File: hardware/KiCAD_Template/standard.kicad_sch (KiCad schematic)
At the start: 40 parts, among them Q1 NMOS, Q2 NPN, SW1 SW_Push, SW2 SW_SPST, U1 ${SIM.PARAMS}

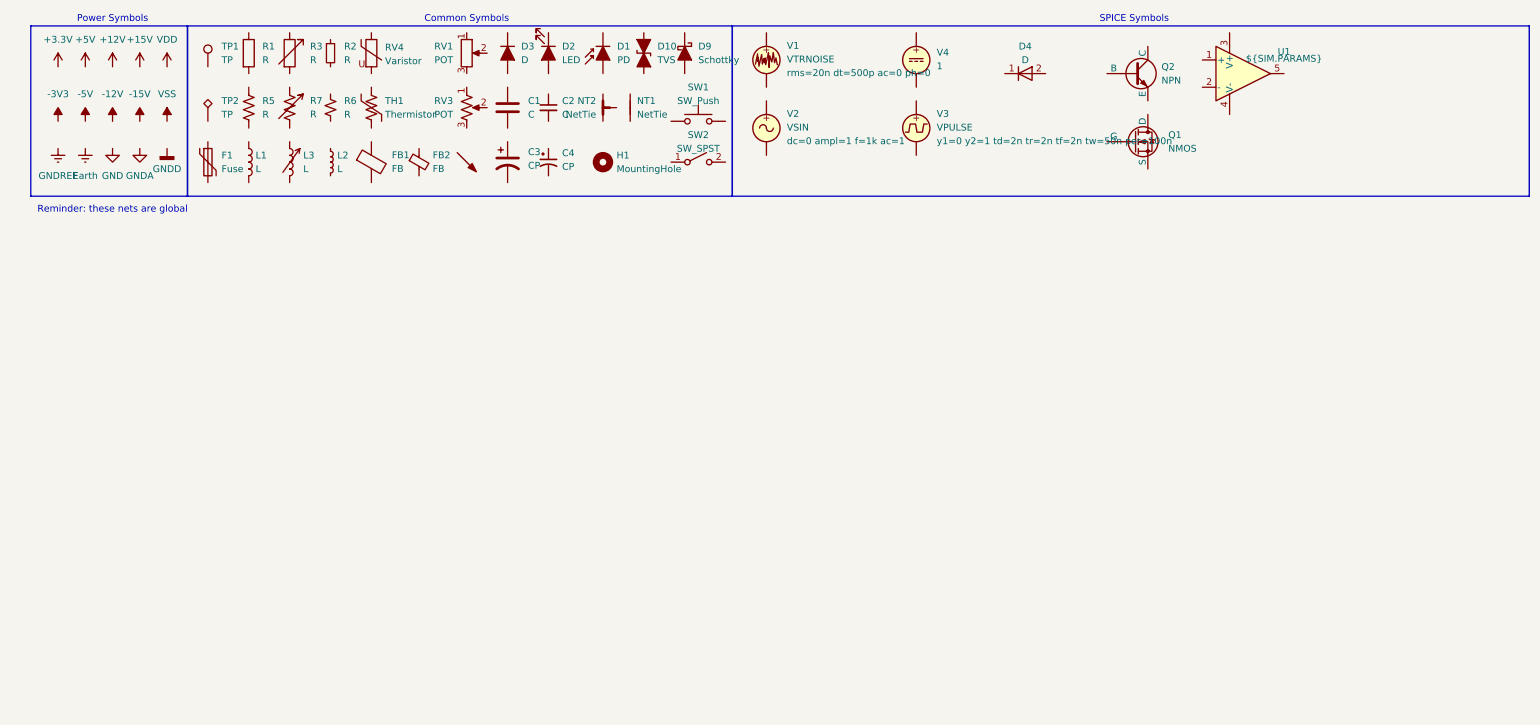
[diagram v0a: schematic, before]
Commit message: fix: kicad build automation output directory
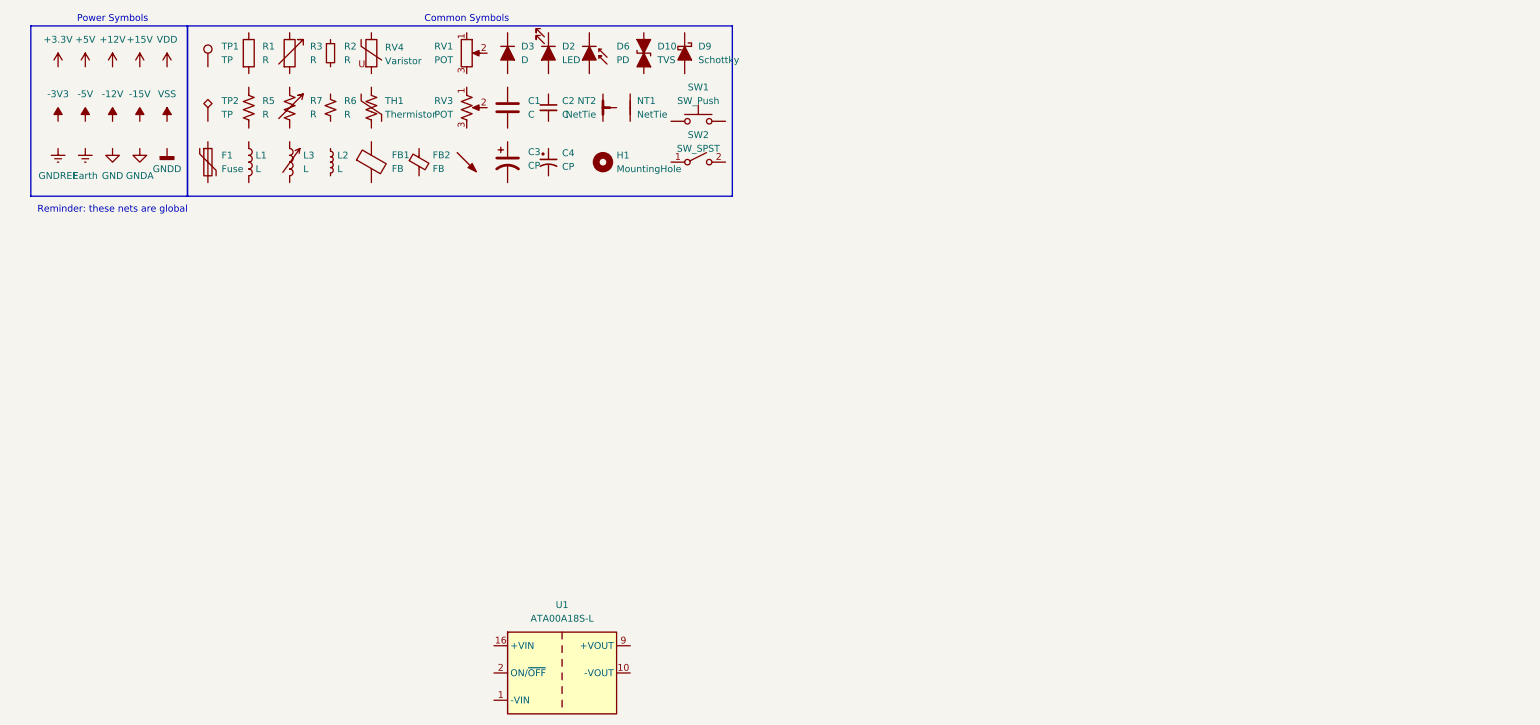
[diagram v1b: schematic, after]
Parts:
- removed D1: PD, symbol Device:D_Photo_Filled
- removed D4: D, symbol Simulation_SPICE:D
- removed Q1: NMOS, symbol Simulation_SPICE:NMOS
- removed Q2: NPN, symbol Simulation_SPICE:NPN
- removed U1: ${SIM.PARAMS}, symbol Simulation_SPICE:OPAMP
- removed V1: VTRNOISE, symbol Simulation_SPICE:VTRNOISE
- removed V2: VSIN, symbol Simulation_SPICE:VSIN
- removed V3: VPULSE, symbol Simulation_SPICE:VPULSE
- removed V4: 1, symbol Simulation_SPICE:VDC
- added D6: PD, symbol Device:D_Photo_Filled
- added U1: ATA00A18S-L, Converter_DCDC:Converter_DCDC_Artesyn_ATA_SMD, symbol Converter_DCDC:ATA00A18S-L
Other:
- note removed: "SPICE Symbols"

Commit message: fix: remove extra symbol on template
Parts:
- removed U1: ATA00A18S-L, Converter_DCDC:Converter_DCDC_Artesyn_ATA_SMD, symbol Converter_DCDC:ATA00A18S-L
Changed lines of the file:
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@@
-	)
-	(symbol
-		(lib_id "Converter_DCDC:ATA00A18S-L")
-		(at 99.06 83.82 0)
-		(unit 1)
-		(exclude_from_sim no)
-		(in_bom yes)
-		(on_board yes)
-		(dnp no)
-		(fields_autoplaced yes)
-		(property "Reference" "U1"
-			(at 99.06 71.12 0)
-			(effects
-				(font
-					(size 1.27 1.27)
-				)
-			)
-		)
-		(property "Value" "ATA00A18S-L"
-			(at 99.06 73.66 0)
-			(effects
-				(font
-					(size 1.27 1.27)
-				)
-			)
-		)
-		(property "Footprint" "Converter_DCDC:Converter_DCDC_Artesyn_ATA_SMD"
-			(at 99.06 92.71 0)
-			(effects
-				(font
-					(size 1.27 1.27)
-					(italic yes)
-				)
-				(hide yes)
-			)
-		)
-		(property "Datasheet" "https://www.artesyn.com/power/assets/ata_series_ds_01apr2015_79c25814fd.pdf"
-			(at 99.06 95.25 0)
-			(effects
-				(font
-					(size 1.27 1.27)
-				)
-				(hide yes)
-			)
-		)
-		(property "Description" "Artesyn 3W Isolated DC/DC Converter Module, 5V Output Voltage, 9-36V Input Voltage"
-			(at 99.06 83.82 0)
-			(effects
-				(font
-					(size 1.27 1.27)
-				)
-				(hide yes)
-			)
-		)
-		(pin "1"
-		)
-		(pin "2"
-		)
-		(pin "7"
-		)
-		(pin "10"
-		)
-		(pin "16"
-		)
-		(pin "9"
-		)
-		(pin "8"
-		)
-		(instances
-			(project ""
-				(path "/dfa2476e-64a0-427c-b480-9f07bad0982f"
-					(reference "U1")
-					(unit 1)
-				)
-			)
-		)
 	)
 	(symbol
